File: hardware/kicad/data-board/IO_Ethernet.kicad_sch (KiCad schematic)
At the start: 44 parts, among them J3 BMS I2C, J8 Conn_01x04, SW1 Wake, U1 TPD4EUSB30, U2 TPD4EUSB30, U3 MagJack-A70-112-331N126, U5 74LVC1G07SE-7, U9 74LVC1G07SE-7

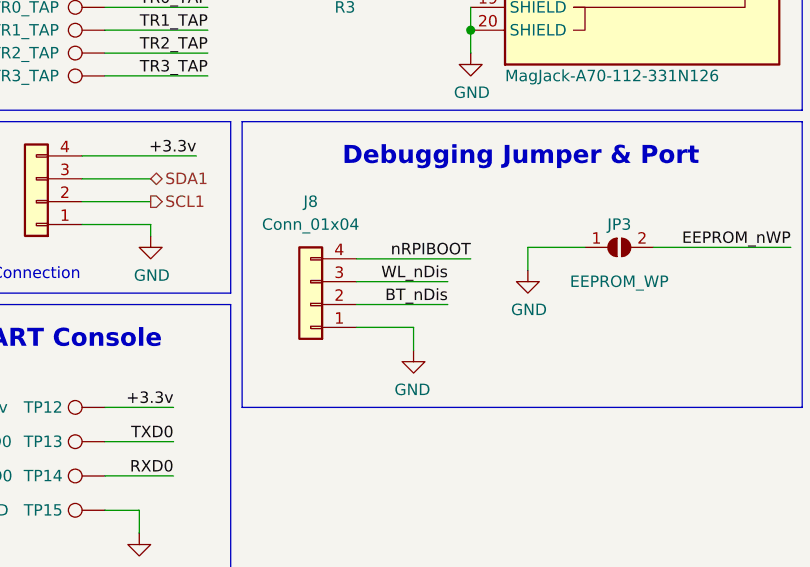
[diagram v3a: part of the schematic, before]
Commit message: update hole to support solder standoff and decrease pogo pin contact hole size
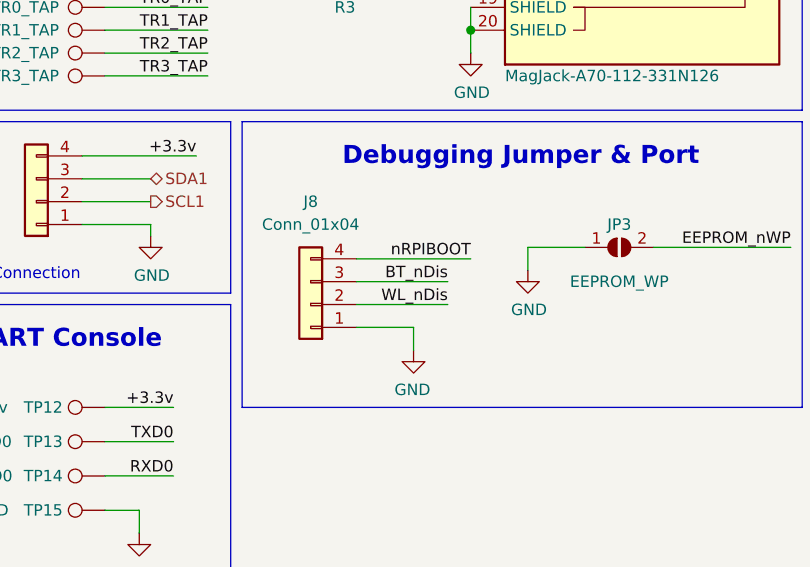
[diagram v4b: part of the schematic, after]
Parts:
- J8: footprint Connector_Molex:Molex_Pico-Lock_504050-0591_1x05-1MP_P1.50mm_Horizontal -> Connector_JST:JST_SH_SM04B-SRSS-TB_1x04-1MP_P1.00mm_Horizontal
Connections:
- net BT_nDis: now also J8.3 (Pin_3); no longer J8.2 (Pin_2)
- net WL_nDis: now also J8.2 (Pin_2); no longer J8.3 (Pin_3)
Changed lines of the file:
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@@
+    (stroke (width 0) (type solid) (color 0 0 0 0))
+  )
+  (wire (pts (xy 233.68 115.57) (xy 243.84 115.57))
+    (stroke (width 0) (type default) (color 0 0 0 0))
+  )
+  (polyline (pts (xy 181.61 82.55) (xy 132.08 82.55))
+    (stroke (width 0) (type solid) (color 0 0 0 0))
+  )
+  (wire (pts (xy 57.15 180.34) (xy 73.66 180.34))
+    (stroke (width 0) (type default) (color 0 0 0 0))
+  )
+  (polyline (pts (xy 219.71 97.79) (xy 219.71 116.84))
+    (stroke (width 0) (type solid) (color 0 0 0 0))
+  )
+  (wire (pts (xy 152.4 133.096) (xy 160.02 133.096))
+    (stroke (width 0) (type solid) (color 0 0 0 0))
+  )
+  (wire (pts (xy 101.346 26.67) (xy 101.346 34.29))
+    (stroke (width 0) (type solid) (color 0 0 0 0))
+  )
+  (polyline (pts (xy 283.21 96.52) (xy 182.88 96.52))
+    (stroke (width 0) (type solid) (color 0 0 0 0))
+  )
+  (wire (pts (xy 39.116 125.73) (xy 39.116 123.19))
+    (stroke (width 0) (type solid) (color 0 0 0 0))
+  )
+  (wire (pts (xy 237.49 41.91) (xy 246.38 41.91))
+    (stroke (width 0) (type solid) (color 0 0 0 0))
+  )
+  (wire (pts (xy 158.75 64.77) (xy 158.75 59.69))
+    (stroke (width 0) (type solid) (color 0 0 0 0))
+  )
+  (polyline (pts (xy 182.88 151.13) (xy 182.88 118.11))
+    (stroke (width 0) (type solid) (color 0 0 0 0))
+  )
+  (polyline (pts (xy 142.24 13.97) (xy 181.61 13.97))
+    (stroke (width 0) (type solid) (color 0 0 0 0))
+  )
+  (wire (pts (xy 116.84 31.75) (xy 116.84 29.21))
+    (stroke (width 0) (type solid) (color 0 0 0 0))
+  )
+  (polyline (pts (xy 219.71 116.84) (xy 182.88 116.84))
+    (stroke (width 0) (type solid) (color 0 0 0 0))
+  )
+  (wire (pts (xy 217.17 80.01) (xy 228.6 80.01))
+    (stroke (width 0) (type solid) (color 0 0 0 0))
+  )
+  (wire (pts (xy 161.3662 52.197) (xy 166.37 52.197))
+    (stroke (width 0) (type solid) (color 0 0 0 0))
+  )
+  (polyline (pts (xy 182.88 97.79) (xy 219.71 97.79))
+    (stroke (width 0) (type solid) (color 0 0 0 0))
+  )
+  (wire (pts (xy 39.116 130.81) (xy 39.116 128.27))
+    (stroke (width 0) (type solid) (color 0 0 0 0))
+  )
+  (polyline (pts (xy 181.61 153.67) (xy 132.08 153.67))
+    (stroke (width 0) (type solid) (color 0 0 0 0))
+  )
+  (wire (pts (xy 101.346 59.69) (xy 101.346 72.39))
+    (stroke (width 0) (type solid) (color 0 0 0 0))
+  )
+  (wire (pts (xy 166.37 52.197) (xy 166.37 53.34))
+    (stroke (width 0) (type solid) (color 0 0 0 0))
+  )
+  (wire (pts (xy 116.84 21.59) (xy 116.84 17.78))
+    (stroke (width 0) (type solid) (color 0 0 0 0))
+  )
+  (wire (pts (xy 219.71 33.02) (xy 227.33 33.02))
+    (stroke (width 0) (type solid) (color 0 0 0 0))
+  )
+  (wire (pts (xy 100.076 100.33) (xy 101.346 100.33))
+    (stroke (width 0) (type solid) (color 0 0 0 0))
+  )
+  (wire (pts (xy 100.076 143.51) (xy 116.586 143.51))
+    (stroke (width 0) (type solid) (color 0 0 0 0))
+  )
+  (wire (pts (xy 37.846 110.49) (xy 39.116 110.49))
+    (stroke (width 0) (type solid) (color 0 0 0 0))
+  )
+  (wire (pts (xy 240.03 123.19) (xy 240.03 120.65))
+    (stroke (width 0) (type default) (color 0 0 0 0))
+  )
+  (wire (pts (xy 100.076 133.35) (xy 114.046 133.35))
+    (stroke (width 0) (type default) (color 0 0 0 0))
+  )
+  (wire (pts (xy 37.846 44.45) (xy 39.116 44.45))
+    (stroke (width 0) (type solid) (color 0 0 0 0))
+  )
+  (polyline (pts (xy 182.88 118.11) (xy 219.71 118.11))
+    (stroke (width 0) (type solid) (color 0 0 0 0))
+  )
+  (polyline (pts (xy 182.88 96.52) (xy 182.88 13.97))
+    (stroke (width 0) (type solid) (color 0 0 0 0))
+  )
+  (wire (pts (xy 100.076 115.57) (xy 100.076 118.11))
+    (stroke (width 0) (type solid) (color 0 0 0 0))
+  )
+  (wire (pts (xy 219.71 27.94) (xy 227.33 27.94))
+    (stroke (width 0) (type solid) (color 0 0 0 0))
+  )
+  (polyline (pts (xy 181.61 31.75) (xy 181.61 82.55))
+    (stroke (width 0) (type solid) (color 0 0 0 0))
+  )
+  (wire (pts (xy 217.17 74.93) (xy 228.6 74.93))
+    (stroke (width 0) (type solid) (color 0 0 0 0))
+  )
+  (wire (pts (xy 39.116 34.29) (xy 37.846 34.29))
+    (stroke (width 0) (type solid) (color 0 0 0 0))
+  )
+  (wire (pts (xy 101.346 34.29) (xy 101.346 46.99))
     (stroke (width 0) (type solid) (color 0 0 0 0))
   )
   (wire (pts (xy 233.68 118.11) (xy 243.84 118.11))
-    (stroke (width 0) (type default) (color 0 0 0 0))
-  )
-  (polyline (pts (xy 181.61 82.55) (xy 132.08 82.55))
-    (stroke (width 0) (type solid) (color 0 0 0 0))
-  )
-  (wire (pts (xy 57.15 180.34) (xy 73.66 180.34))
-    (stroke (width 0) (type default) (color 0 0 0 0))
-  )
-  (polyline (pts (xy 219.71 97.79) (xy 219.71 116.84))
-    (stroke (width 0) (type solid) (color 0 0 0 0))
-  )
-  (wire (pts (xy 152.4 133.096) (xy 160.02 133.096))
-    (stroke (width 0) (type solid) (color 0 0 0 0))
-  )
-  (wire (pts (xy 101.346 26.67) (xy 101.346 34.29))
-    (stroke (width 0) (type solid) (color 0 0 0 0))
-  )
-  (polyline (pts (xy 283.21 96.52) (xy 182.88 96.52))
-    (stroke (width 0) (type solid) (color 0 0 0 0))
-  )
-  (wire (pts (xy 39.116 125.73) (xy 39.116 123.19))
-    (stroke (width 0) (type solid) (color 0 0 0 0))
-  )
-  (wire (pts (xy 237.49 41.91) (xy 246.38 41.91))
-    (stroke (width 0) (type solid) (color 0 0 0 0))
-  )
-  (wire (pts (xy 158.75 64.77) (xy 158.75 59.69))
-    (stroke (width 0) (type solid) (color 0 0 0 0))
-  )
-  (polyline (pts (xy 182.88 151.13) (xy 182.88 118.11))
-    (stroke (width 0) (type solid) (color 0 0 0 0))
-  )
-  (polyline (pts (xy 142.24 13.97) (xy 181.61 13.97))
-    (stroke (width 0) (type solid) (color 0 0 0 0))
-  )
-  (wire (pts (xy 116.84 31.75) (xy 116.84 29.21))
-    (stroke (width 0) (type solid) (color 0 0 0 0))
-  )
-  (polyline (pts (xy 219.71 116.84) (xy 182.88 116.84))
-    (stroke (width 0) (type solid) (color 0 0 0 0))
-  )
-  (wire (pts (xy 217.17 80.01) (xy 228.6 80.01))
-    (stroke (width 0) (type solid) (color 0 0 0 0))
-  )
-  (wire (pts (xy 161.3662 52.197) (xy 166.37 52.197))
-    (stroke (width 0) (type solid) (color 0 0 0 0))
-  )
-  (polyline (pts (xy 182.88 97.79) (xy 219.71 97.79))
-    (stroke (width 0) (type solid) (color 0 0 0 0))
-  )
-  (wire (pts (xy 39.116 130.81) (xy 39.116 128.27))
-    (stroke (width 0) (type solid) (color 0 0 0 0))
-  )
-  (polyline (pts (xy 181.61 153.67) (xy 132.08 153.67))
-    (stroke (width 0) (type solid) (color 0 0 0 0))
-  )
-  (wire (pts (xy 101.346 59.69) (xy 101.346 72.39))
-    (stroke (width 0) (type solid) (color 0 0 0 0))
-  )
-  (wire (pts (xy 166.37 52.197) (xy 166.37 53.34))
-    (stroke (width 0) (type solid) (color 0 0 0 0))
-  )
-  (wire (pts (xy 116.84 21.59) (xy 116.84 17.78))
-    (stroke (width 0) (type solid) (color 0 0 0 0))
-  )
-  (wire (pts (xy 219.71 33.02) (xy 227.33 33.02))
-    (stroke (width 0) (type solid) (color 0 0 0 0))
-  )
-  (wire (pts (xy 100.076 100.33) (xy 101.346 100.33))
-    (stroke (width 0) (type solid) (color 0 0 0 0))
-  )
-  (wire (pts (xy 100.076 143.51) (xy 116.586 143.51))
-    (stroke (width 0) (type solid) (color 0 0 0 0))
-  )
-  (wire (pts (xy 37.846 110.49) (xy 39.116 110.49))
-    (stroke (width 0) (type solid) (color 0 0 0 0))
-  )
-  (wire (pts (xy 240.03 123.19) (xy 240.03 120.65))
-    (stroke (width 0) (type default) (color 0 0 0 0))
-  )
-  (wire (pts (xy 100.076 133.35) (xy 114.046 133.35))
-    (stroke (width 0) (type default) (color 0 0 0 0))
-  )
-  (wire (pts (xy 37.846 44.45) (xy 39.116 44.45))
-    (stroke (width 0) (type solid) (color 0 0 0 0))
-  )
-  (polyline (pts (xy 182.88 118.11) (xy 219.71 118.11))
-    (stroke (width 0) (type solid) (color 0 0 0 0))
-  )
-  (polyline (pts (xy 182.88 96.52) (xy 182.88 13.97))
-    (stroke (width 0) (type solid) (color 0 0 0 0))
-  )
-  (wire (pts (xy 100.076 115.57) (xy 100.076 118.11))
-    (stroke (width 0) (type solid) (color 0 0 0 0))
-  )
-  (wire (pts (xy 219.71 27.94) (xy 227.33 27.94))
-    (stroke (width 0) (type solid) (color 0 0 0 0))
-  )
-  (polyline (pts (xy 181.61 31.75) (xy 181.61 82.55))
-    (stroke (width 0) (type solid) (color 0 0 0 0))
-  )
-  (wire (pts (xy 217.17 74.93) (xy 228.6 74.93))
-    (stroke (width 0) (type solid) (color 0 0 0 0))
-  )
-  (wire (pts (xy 39.116 34.29) (xy 37.846 34.29))
-    (stroke (width 0) (type solid) (color 0 0 0 0))
-  )
-  (wire (pts (xy 101.346 34.29) (xy 101.346 46.99))
-    (stroke (width 0) (type solid) (color 0 0 0 0))
-  )
-  (wire (pts (xy 233.68 115.57) (xy 243.84 115.57))
     (stroke (width 0) (type default) (color 0 0 0 0))
   )
@@
   )
   (text "TODO: Invvestigate. Pull-up might not be needed here."
-    (at 180.848 153.035 0)
+    (at 180.848 153.035 180)
     (effects (font (size 0.64 0.64)) (justify right bottom))
   )
@@
     (effects (font (size 1.27 1.27)) (justify right bottom))
   )
-  (label "BT_nDis" (at 243.84 118.11 180)
+  (label "BT_nDis" (at 243.84 115.57 180)
     (effects (font (size 1.27 1.27)) (justify right bottom))
   )
@@
     (effects (font (size 2.0066 2.0066)) (justify left bottom))
   )
-  (label "WL_nDis" (at 243.84 115.57 180)
+  (label "WL_nDis" (at 243.84 118.11 180)
     (effects (font (size 1.27 1.27)) (justify right bottom))
   )
@@
     (property "Reference" "J8" (id 0) (at 228.6 106.68 0))
     (property "Value" "Conn_01x04" (id 1) (at 228.6 109.22 0))
-    (property "Footprint" "Connector_Molex:Molex_Pico-Lock_504050-0591_1x05-1MP_P1.50mm_Horizontal" (id 2) (at 228.6 118.11 0)
-      (effects (font (size 1.27 1.27)) hide)
-    )
+    (property "Footprint" "Connector_JST:JST_SH_SM04B-SRSS-TB_1x04-1MP_P1.00mm_Horizontal" (id 2) (at 228.6 118.11 0)
+      (effects (font (size 1.27 1.27)) hide)
+    )

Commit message: hardware/kicad/data-board/SWARM.kicad_sch
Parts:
- removed J3: BMS I2C, Connector_PinHeader_2.54mm:PinHeader_1x04_P2.54mm_Vertical, symbol Connector_Generic:Conn_01x04
- added J3: Power Controller, Teapot:PogoPinContact_2_P4.8mm_D2.3mm_H0.7mm, symbol Connector_Generic:Conn_01x02
- J8: Manufacturer Link (none) -> https://www.lcsc.com/product-detail/Wire-To-Board-Wire-To-W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
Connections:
- net SCL1: now also J3.1 (Pin_1)
- net SDA1: now also J3.2 (Pin_2)
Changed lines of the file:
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@@
     (stroke (width 0) (type solid) (color 0 0 0 0))
-  )
-  (wire (pts (xy 210.82 110.49) (xy 210.82 109.22))
-    (stroke (width 0) (type default) (color 0 0 0 0))
   )
   (wire (pts (xy 34.29 49.53) (xy 39.116 49.53))
@@
     (stroke (width 0) (type solid) (color 0 0 0 0))
   )
-  (wire (pts (xy 203.2 109.22) (xy 210.82 109.22))
-    (stroke (width 0) (type default) (color 0 0 0 0))
-  )
   (polyline (pts (xy 132.08 83.82) (xy 181.61 83.82))
     (stroke (width 0) (type solid) (color 0 0 0 0))
@@
     (stroke (width 0) (type solid) (color 0 0 0 0))
   )
-  (wire (pts (xy 203.2 101.6) (xy 215.9 101.6))
-    (stroke (width 0) (type default) (color 0 0 0 0))
-  )
   (wire (pts (xy 219.71 59.69) (xy 228.6 59.69))
     (stroke (width 0) (type solid) (color 0 0 0 0))
@@
     (stroke (width 0) (type solid) (color 0 0 0 0))
   )
-  (wire (pts (xy 203.2 106.68) (xy 210.82 106.68))
+  (wire (pts (xy 203.2 106.045) (xy 210.82 106.045))
     (stroke (width 0) (type default) (color 0 0 0 0))
   )
@@
     (stroke (width 0) (type solid) (color 0 0 0 0))
   )
-  (wire (pts (xy 203.2 104.14) (xy 210.82 104.14))
+  (wire (pts (xy 203.2 103.505) (xy 210.82 103.505))
     (stroke (width 0) (type default) (color 0 0 0 0))
   )
@@
     (effects (font (size 1.27 1.27)) (justify right bottom))
   )
-  (label "+3.3v" (at 215.9 101.6 180)
-    (effects (font (size 1.27 1.27)) (justify right bottom))
-  )
   (label "TR2_TAP" (at 246.38 64.77 180)
     (effects (font (size 1.27 1.27)) (justify right bottom))
@@
     (effects (font (size 1.27 1.27)) (justify left))
   )
-  (hierarchical_label "SCL1" (shape output) (at 210.82 106.68 0)
+  (hierarchical_label "SCL1" (shape output) (at 210.82 106.045 0)
     (effects (font (size 1.27 1.27)) (justify left))
   )
@@
     (effects (font (size 1.27 1.27)) (justify left))
   )
-  (hierarchical_label "SDA1" (shape bidirectional) (at 210.82 104.14 0)
+  (hierarchical_label "SDA1" (shape bidirectional) (at 210.82 103.505 0)
     (effects (font (size 1.27 1.27)) (justify left))
   )
@@
     (pin "1")
   )
+  (symbol (lib_id "Connector_Generic:Conn_01x02") (at 198.12 106.045 180) (unit 1)
+    (in_bom yes) (on_board yes)
+    (property "Reference" "J3" (id 0) (at 194.945 104.14 0))
+    (property "Value" "Power Controller" (id 1) (at 193.675 109.855 0))
+    (property "Footprint" "Teapot:PogoPinContact_2_P4.8mm_D2.3mm_H0.7mm" (id 2) (at 198.12 106.045 0)
+      (effects (font (size 1.27 1.27)) hide)
+    )
+    (property "Datasheet" "~" (id 3) (at 198.12 106.045 0)
+      (effects (font (size 1.27 1.27)) hide)
+    )
+    (pin "1")
+    (pin "2")
+  )
   (symbol (lib_id "Device:R") (at 152.4 138.43 0) (unit 1)
     (in_bom yes) (on_board yes)
@@
     )
     (property "Datasheet" "~" (id 3) (at 154.94 110.49 0)
-      (effects (font (size 1.27 1.27)) hide)
-    )
-    (pin "1")
-  )
-  (symbol (lib_id "power:GND") (at 210.82 110.49 0) (unit 1)
-    (in_bom yes) (on_board yes)
-    (property "Reference" "#PWR0135" (id 0) (at 210.82 116.84 0)
-      (effects (font (size 1.27 1.27)) hide)
-    )
-    (property "Value" "GND" (id 1) (at 210.947 114.8842 0))
-    (property "Footprint" "" (id 2) (at 210.82 110.49 0)
-      (effects (font (size 1.27 1.27)) hide)
-    )
-    (property "Datasheet" "" (id 3) (at 210.82 110.49 0)
       (effects (font (size 1.27 1.27)) hide)
     )
@@
     (pin "200")
   )
-  (symbol (lib_id "Connector_Generic:Conn_01x04") (at 198.12 106.68 180) (unit 1)
-    (in_bom yes) (on_board yes)
-    (property "Reference" "J3" (id 0) (at 191.77 101.6 0))
-    (property "Value" "BMS I2C" (id 1) (at 190.5 104.14 0))
-    (property "Footprint" "Connector_PinHeader_2.54mm:PinHeader_1x04_P2.54mm_Vertical" (id 2) (at 198.12 106.68 0)
-      (effects (font (size 1.27 1.27)) hide)
-    )
-    (property "Datasheet" "~" (id 3) (at 198.12 106.68 0)
-      (effects (font (size 1.27 1.27)) hide)
-    )
-    (pin "1")
-    (pin "2")
-    (pin "3")
-    (pin "4")
-  )
   (symbol (lib_id "Connector:TestPoint") (at 154.94 107.95 90) (unit 1)
     (in_bom yes) (on_board yes)
@@
       (effects (font (size 1.27 1.27)) hide)
     )
+    (property "Manufacturer Link" "https://www.lcsc.com/product-detail/Wire-To-Board-Wire-To-Wire-Connector_JST-Sales-America-SM04B-SRSS-TB-LF-SN_C160404.html" (id 4) (at 228.6 118.11 0)
+      (effects (font (size 1.27 1.27)) hide)
+    )
